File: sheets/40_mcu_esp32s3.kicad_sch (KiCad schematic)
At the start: 20 parts, among them J401 USB4105-GF-A, J402 UART0, SW401 RESET, SW402 BOOT, U401 ESP32-S3-WROOM-1-N8R2, U402 USBLC6-2SC6

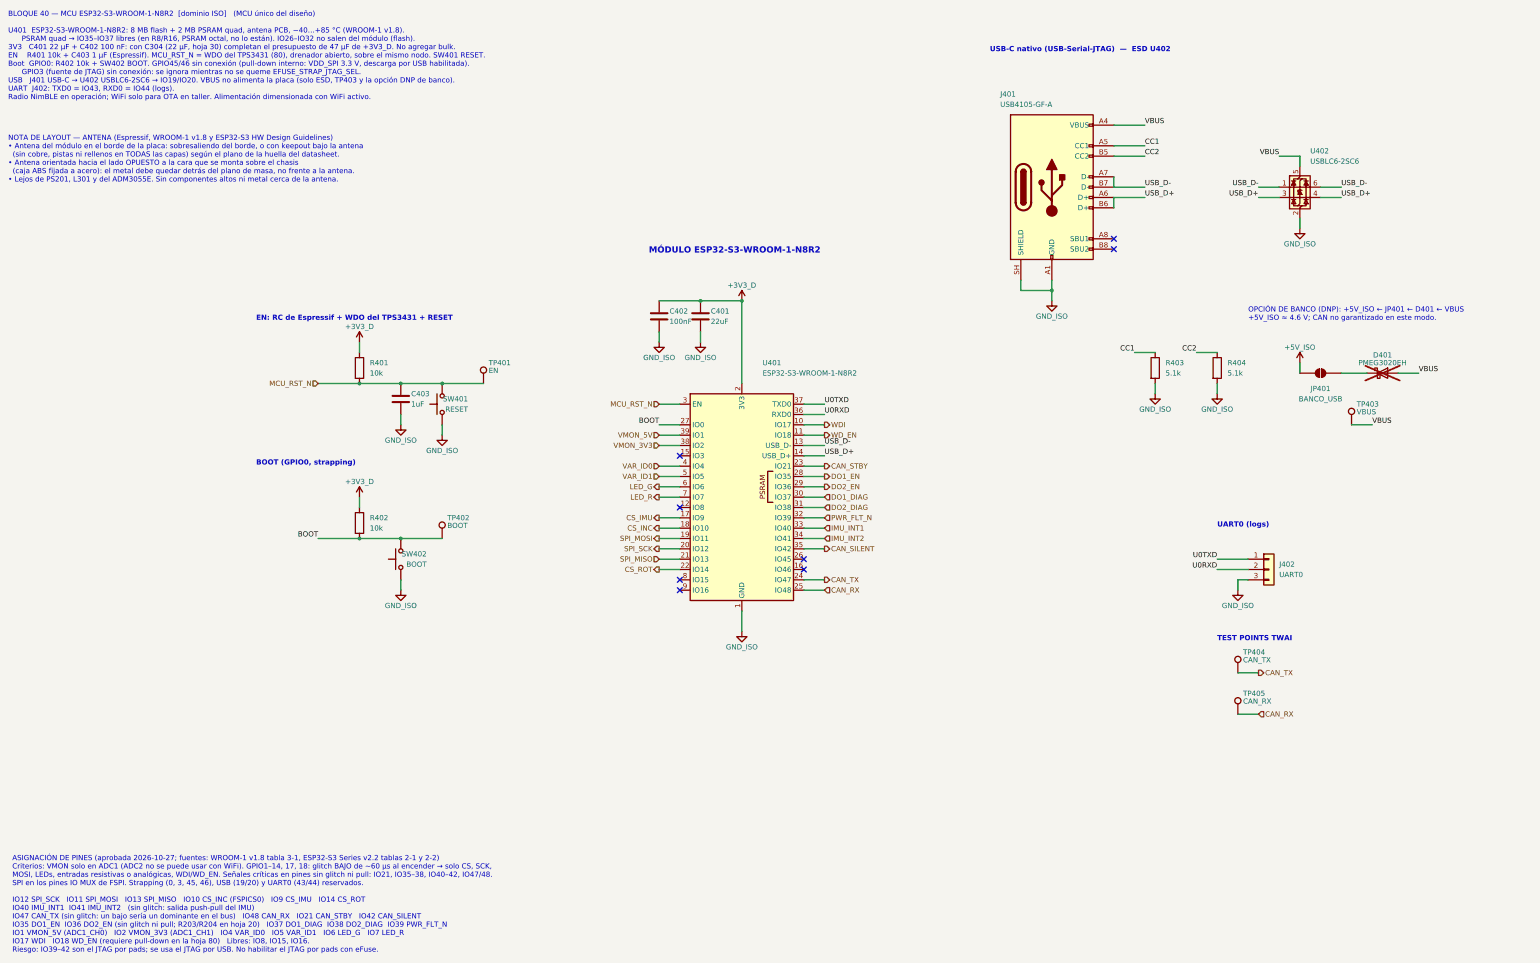
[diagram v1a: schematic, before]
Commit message: [Claude Code] 20_buck_5v: opción B (no aislada) con LMR38010; masas unificadas
- sheets/20_isolation -> sheets/20_buck_5v: se quitan PS201, ISO7763 y
  TPS7A1650; U201 LMR38010SQDDARQ1 (PROTO: LMR38010SDDAR, LCSC C5219310),
  5.02 V / 1 A a 400 kHz según TI SNVSC73B (L201 XAL6060-333, 3 x 22 uF,
  RT 64.9k, FB 100k/24.9k). Huella oficial HSOIC-8 con vías térmicas.
- Símbolo LMR38010 (easyeda2kicad) en lib/easyeda2kicad/INCLI-VA_easyeda,
  con tipos de pin ajustados; registrado en sym-lib-table.
- Todas las hojas: GND_ISO -> GND_VEH, +5V_ISO -> +5V_VEH.
- Raíz: EN/DIAG/FLT directos entre las hojas 40, 70 y 10; la hoja 20 sin pines.
- 10_power_input: R111 a +3V3_D, C109 = 100 nF (inrush con C105),
  C105 DNP solo en PROTO; se quita un PWR_FLAG suelto en GND_VEH.
- 70_output_ch: cambios de layout del usuario (hechos en KiCad).
- Textos de las hojas 30/40/50/80 y la raíz sin referencias al aislamiento.
- ERC: 0 en 10, 20, 30, 40, 50, 60 y 70; quedan los de 80 (hoja vacía).

Co-Authored-By: Claude Opus 5.5 <noreply@anthropic.com>
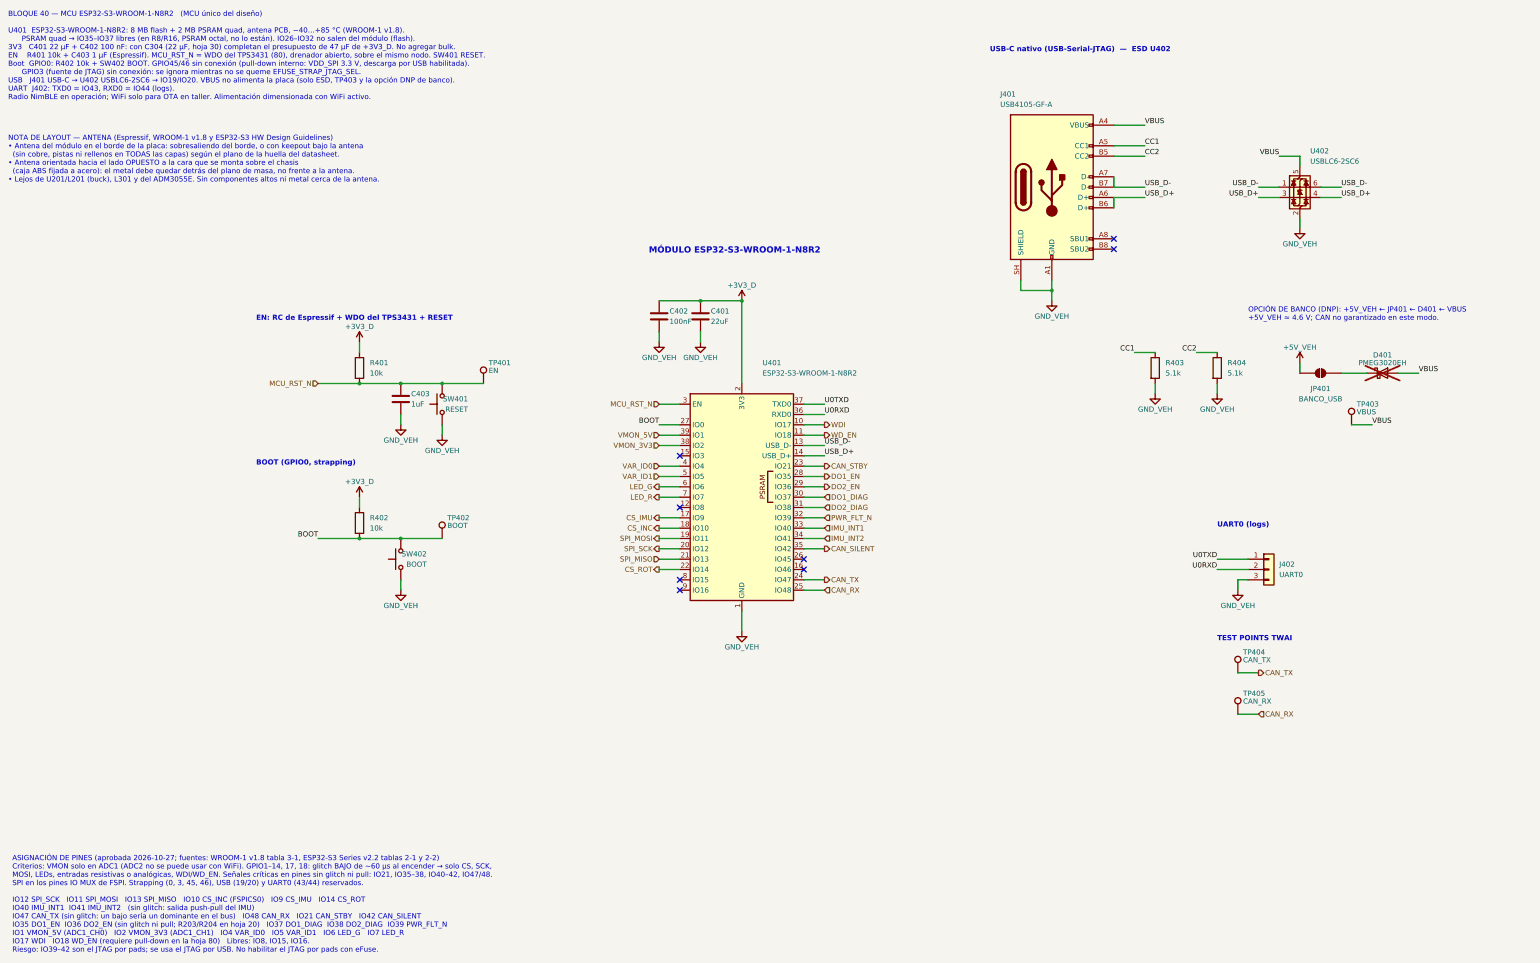
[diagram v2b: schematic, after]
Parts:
- D401: Notes DNP. Opción de banco: alimenta +5V_ISO desde VBUS para flas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 -> DNP. Opción de banco: alimenta +5V_VEH desde VBUS para flas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
- J401: Notes USB-C solo USB 2.0 para el USB-Serial-JTAG del ESP32-S3 (GPIO19/20). Programación, consola y JTAG. Masa = GND_ISO: la PC queda aislada del vehículo por la barrera 1. Blindaje a GND_ISO. -> USB-C solo USB 2.0 para el USB-Serial-JTAG del ESP32-S3 (GPIO19/20). Programación, consola y JTAG. Masa = GND_VEH: SIN aislamiento (opción B), la PC comparte masa con el vehículo; en el vehículo usar aislador USB/UART o laptop a batería. Blindaje a GND_VEH.
- J402: Notes UART0 para logs: 1 = TXD0 (IO43, sale del MCU), 2 = RXD0 (IO44), 3 = GND_ISO. Adaptador USB-UART de 3.3 V. -> UART0 para logs: 1 = TXD0 (IO43, sale del MCU), 2 = RXD0 (IO44), 3 = GND_VEH. Adaptador USB-UART de 3.3 V.
- JP401: Notes Abierto de fábrica. Cerrar solo en el banco, junto con D401, para alimentar +5V_ISO desde USB. Abrir antes de instalar en el vehículo. -> Abierto de fábrica. Cerrar solo en el banco, junto con D401, para alimentar +5V_VEH desde USB. Abrir antes de instalar en el vehículo.
- SW401: Notes Botón RESET: lleva EN a GND_ISO. THT 6 x 6 mm, fácil de sol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 -> Botón RESET: lleva EN a GND_VEH. THT 6 x 6 mm, fácil de sol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
- SW402: Notes Botón BOOT: GPIO0 a GND_ISO. Mantener apretado y soltar RES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 -> Botón BOOT: GPIO0 a GND_VEH. Mantener apretado y soltar RES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
- U401: Notes 8 MB flash quad + 2 MB PSRAM quad, antena PCB, -40 a +85 C (las variantes R8/R16 con PSRAM octal llegan solo a 65 C). PSRAM quad: IO35-IO37 libres (WROOM-1 v1.8, tabla 3-1, nota b). LCSC C2913204. Pad 41 (EPAD) y pines 1/40 a GND_ISO. Antena al borde de la placa con keepout (ver nota de layout). -> 8 MB flash quad + 2 MB PSRAM quad, antena PCB, -40 a +85 C (las variantes R8/R16 con PSRAM octal llegan solo a 65 C). PSRAM quad: IO35-IO37 libres (WROOM-1 v1.8, tabla 3-1, nota b). LCSC C2913204. Pad 41 (EPAD) y pines 1/40 a GND_VEH. Antena al borde de la placa con keepout (ver nota de layout).
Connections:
- net +5V_ISO renamed +5V_VEH
- net GND_ISO renamed GND_VEH
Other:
- note added: "BLOQUE 40 — MCU ESP32-S3-WROOM-1-N8R2 (MCU único del diseño) U401 ESP32-S3-WROOM-1-N8R2: 8 MB flash + 2 MB PSRAM quad, antena PCB, −40…+85 °C (WROOM-1 v1.8). PSRAM quad → IO35–IO37 libres (en R8/R16, PSRAM octal, no lo están). IO26–IO32 no salen del módulo (flash). 3V3 C401 22 µF + C402 100 nF: con C304 (22 µF, hoja 30) completan el presupuesto de 47 µF de +3V3_D. No agregar bulk. EN R401 10k + C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"
- note added: "OPCIÓN DE BANCO (DNP): +5V_VEH ← JP401 ← D401 ← VBUS +5V_VEH ≈ 4.6 V; CAN no garantizado en este modo."
- note removed: "BLOQUE 40 — MCU ESP32-S3-WROOM-1-N8R2 [dominio ISO] (MCU único del diseño) U401 ESP32-S3-WROOM-1-N8R2: 8 MB flash + 2 MB PSRAM quad, antena PCB, −40…+85 °C (WROOM-1 v1.8). PSRAM quad → IO35–IO37 libres (en R8/R16, PSRAM octal, no lo están). IO26–IO32 no salen del módulo (flash). 3V3 C401 22 µF + C402 100 nF: con C304 (22 µF, hoja 30) completan el presupuesto de 47 µF de +3V3_D. No agregar bulk. E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"
- note removed: "OPCIÓN DE BANCO (DNP): +5V_ISO ← JP401 ← D401 ← VBUS +5V_ISO ≈ 4.6 V; CAN no garantizado en este modo."
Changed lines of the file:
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@@
 		)
 	)
-	(text "OPCIÓN DE BANCO (DNP): +5V_ISO ← JP401 ← D401 ← VBUS\n+5V_ISO ≈ 4.6 V; CAN no garantizado en este modo."
+	(text "OPCIÓN DE BANCO (DNP): +5V_VEH ← JP401 ← D401 ← VBUS\n+5V_VEH ≈ 4.6 V; CAN no garantizado en este modo."
 		(exclude_from_sim no)
 		(at 325.12 96.52 0)
@@
 		)
 	)
-	(text "NOTA DE LAYOUT — ANTENA (Espressif, WROOM-1 v1.8 y ESP32-S3 HW Design Guidelines)\n• Antena del módulo en el borde de la placa: sobresaliendo del borde, o con keepout bajo la antena\n  (sin cobre, pistas ni rellenos en TODAS las capas) según el plano de la huella del datasheet.\n• Antena orientada hacia el lado OPUESTO a la cara que se monta sobre el chasis\n  (caja ABS fijada a acero): el metal debe quedar detrás del plano de masa, no frente a la antena.\n• Lejos de PS201, L301 y del ADM3055E. Sin componentes altos ni metal cerca de la antena."
+	(text "NOTA DE LAYOUT — ANTENA (Espressif, WROOM-1 v1.8 y ESP32-S3 HW Design Guidelines)\n• Antena del módulo en el borde de la placa: sobresaliendo del borde, o con keepout bajo la antena\n  (sin cobre, pistas ni rellenos en TODAS las capas) según el plano de la huella del datasheet.\n• Antena orientada hacia el lado OPUESTO a la cara que se monta sobre el chasis\n  (caja ABS fijada a acero): el metal debe quedar detrás del plano de masa, no frente a la antena.\n• Lejos de U201/L201 (buck), L301 y del ADM3055E. Sin componentes altos ni metal cerca de la antena."
 		(exclude_from_sim no)
 		(at 20.32 50.8 0)
@@
 		)
 	)
-	(text "BLOQUE 40 — MCU ESP32-S3-WROOM-1-N8R2  [dominio ISO]   (MCU único del diseño)\n\nU401  ESP32-S3-WROOM-1-N8R2: 8 MB flash + 2 MB PSRAM quad, antena PCB, −40…+85 °C (WROOM-1 v1.8).\n      PSRAM quad → IO35–IO37 libres (en R8/R16, PSRAM octal, no lo están). IO26–IO32 no salen del módulo (flash).\n3V3   C401 22 µF + C402 100 nF: con C304 (22 µF, hoja 30) completan el presupuesto de 47 µF de +3V3_D. No agregar bulk.\nEN    R401 10k + C403 1 µF (Espressif). MCU_RST_N = WDO del TPS3431 (80), drenador abierto, sobre el mismo nodo. SW401 RESET.\nBoot  GPIO0: R402 10k + SW402 BOOT. GPIO45/46 sin conexión (pull-down interno: VDD_SPI 3.3 V, descarga por USB habilitada).\n      GPIO3 (fuente de JTAG) sin conexión: se ignora mientras no se queme EFUSE_STRAP_JTAG_SEL.\nUSB   J401 USB-C → U402 USBLC6-2SC6 → IO19/IO20. VBUS no alimenta la placa (solo ESD, TP403 y la opción DNP de banco).\nUART  J402: TXD0 = IO43, RXD0 = IO44 (logs).\nRadio NimBLE en operación; WiFi solo para OTA en taller. Alimentación dimensionada con WiFi activo."
+	(text "BLOQUE 40 — MCU ESP32-S3-WROOM-1-N8R2   (MCU único del diseño)\n\nU401  ESP32-S3-WROOM-1-N8R2: 8 MB flash + 2 MB PSRAM quad, antena PCB, −40…+85 °C (WROOM-1 v1.8).\n      PSRAM quad → IO35–IO37 libres (en R8/R16, PSRAM octal, no lo están). IO26–IO32 no salen del módulo (flash).\n3V3   C401 22 µF + C402 100 nF: con C304 (22 µF, hoja 30) completan el presupuesto de 47 µF de +3V3_D. No agregar bulk.\nEN    R401 10k + C403 1 µF (Espressif). MCU_RST_N = WDO del TPS3431 (80), drenador abierto, sobre el mismo nodo. SW401 RESET.\nBoot  GPIO0: R402 10k + SW402 BOOT. GPIO45/46 sin conexión (pull-down interno: VDD_SPI 3.3 V, descarga por USB habilitada).\n      GPIO3 (fuente de JTAG) sin conexión: se ignora mientras no se queme EFUSE_STRAP_JTAG_SEL.\nUSB   J401 USB-C → U402 USBLC6-2SC6 → IO19/IO20. VBUS no alimenta la placa (solo ESD, TP403 y la opción DNP de banco).\nUART  J402: TXD0 = IO43, RXD0 = IO44 (logs).\nRadio NimBLE en operación; WiFi solo para OTA en taller. Alimentación dimensionada con WiFi activo."
 		(exclude_from_sim no)
 		(at 20.32 20.32 0)
@@
 	)
 	(symbol
-		(lib_id "INCLI-VA:GND_ISO")
+		(lib_id "INCLI-VA:GND_VEH")
 		(at 322.58 162.56 0)
 		(unit 1)
@@
 			)
 		)
-		(property "Value" "GND_ISO"
+		(property "Value" "GND_VEH"
 			(at 322.58 166.37 0)
 			(show_name no)
@@
 	)
 	(symbol
-		(lib_id "INCLI-VA:GND_ISO")
+		(lib_id "INCLI-VA:GND_VEH")
 		(at 116.84 121.92 0)
 		(unit 1)
@@
 			)
 		)
-		(property "Value" "GND_ISO"
+		(property "Value" "GND_VEH"
 			(at 116.84 125.73 0)
 			(show_name no)
@@
 	)
 	(symbol
-		(lib_id "INCLI-VA:GND_ISO")
+		(lib_id "INCLI-VA:GND_VEH")
 		(at 200.66 172.72 0)
 		(unit 1)
@@
 			)
 		)
-		(property "Value" "GND_ISO"
+		(property "Value" "GND_VEH"
 			(at 200.66 176.53 0)
 			(show_name no)
@@
 	)
 	(symbol
-		(lib_id "INCLI-VA:GND_ISO")
+		(lib_id "INCLI-VA:GND_VEH")
 		(at 317.5 114.3 0)
 		(unit 1)
@@
 			)
 		)
-		(property "Value" "GND_ISO"
+		(property "Value" "GND_VEH"
 			(at 317.5 118.11 0)
 			(show_name no)
@@
 	)
 	(symbol
-		(lib_id "INCLI-VA:GND_ISO")
+		(lib_id "INCLI-VA:GND_VEH")
 		(at 180.34 101.6 0)
 		(unit 1)
@@
 			)
 		)
-		(property "Value" "GND_ISO"
+		(property "Value" "GND_VEH"
 			(at 180.34 105.41 0)
 			(show_name no)
@@
 			)
 		)
-		(property "Notes" "8 MB flash quad + 2 MB PSRAM quad, antena PCB, -40 a +85 C (las variantes R8/R16 con PSRAM octal llegan solo a 65 C). PSRAM quad: IO35-IO37 libres (WROOM-1 v1.8, tabla 3-1, nota b). LCSC C2913204. Pad 41 (EPAD) y pines 1/40 a GND_ISO. Antena al borde de la placa con keepout (ver nota de layout)."
+		(property "Notes" "8 MB flash quad + 2 MB PSRAM quad, antena PCB, -40 a +85 C (las variantes R8/R16 con PSRAM octal llegan solo a 65 C). PSRAM quad: IO35-IO37 libres (WROOM-1 v1.8, tabla 3-1, nota b). LCSC C2913204. Pad 41 (EPAD) y pines 1/40 a GND_VEH. Antena al borde de la placa con keepout (ver nota de layout)."
 			(at 200.66 139.7 0)
 			(hide yes)
@@
 			)
 		)
-		(property "Notes" "Botón BOOT: GPIO0 a GND_ISO. Mantener apretado y soltar RESET para entrar en descarga."
+		(property "Notes" "Botón BOOT: GPIO0 a GND_VEH. Mantener apretado y soltar RESET para entrar en descarga."
 			(at 116.84 154.94 0)
 			(hide yes)
@@
 			)
 		)
-		(property "Notes" "DNP. Opción de banco: alimenta +5V_ISO desde VBUS para flashear sin vehículo (cerrar JP401). +5V_ISO queda en ~4.6 V: el CAN (ADM3055E, VCC mín. 4.5 V) no está garantizado en este modo. Limitar la carga a lo que entrega el puerto (WiFi apagado). Con PS201 activo el diodo queda en inversa. MPN a verificar (disponibilidad y especificación) antes de congelar el BOM."
+		(property "Notes" "DNP. Opción de banco: alimenta +5V_VEH desde VBUS para flashear sin vehículo (cerrar JP401). +5V_VEH queda en ~4.6 V: el CAN (ADM3055E, VCC mín. 4.5 V) no está garantizado en este modo. Limitar la carga a lo que entrega el puerto (WiFi apagado). Con el buck activo el diodo queda en inversa. MPN a verificar (disponibilidad y especificación) antes de congelar el BOM."
 			(at 358.14 109.22 0)
 			(hide yes)
@@
 			)
 		)
-		(property "Notes" "Abierto de fábrica. Cerrar solo en el banco, junto con D401, para alimentar +5V_ISO desde USB. Abrir antes de instalar en el vehículo."
+		(property "Notes" "Abierto de fábrica. Cerrar solo en el banco, junto con D401, para alimentar +5V_VEH desde USB. Abrir antes de instalar en el vehículo."
 			(at 342.9 109.22 0)
 			(hide yes)
@@
 	)
 	(symbol
-		(lib_id "INCLI-VA:GND_ISO")
+		(lib_id "INCLI-VA:GND_VEH")
 		(at 190.5 101.6 0)
 		(unit 1)
@@
 			)
 		)
-		(property "Value" "GND_ISO"
+		(property "Value" "GND_VEH"
 			(at 190.5 105.41 0)
 			(show_name no)
@@
 			)
 		)
-		(property "Notes" "UART0 para logs: 1 = TXD0 (IO43, sale del MCU), 2 = RXD0 (IO44), 3 = GND_ISO. Adaptador USB-UART de 3.3 V."
+		(property "Notes" "UART0 para logs: 1 = TXD0 (IO43, sale del MCU), 2 = RXD0 (IO44), 3 = GND_VEH. Adaptador USB-UART de 3.3 V."
 			(at 330.2 157.48 0)
 			(hide yes)
@@
 	)
 	(symbol
-		(lib_id "INCLI-VA:GND_ISO")
+		(lib_id "INCLI-VA:GND_VEH")
 		(at 276.86 91.44 0)
 		(unit 1)
@@
 			)
 		)
-		(property "Value" "GND_ISO"
+		(property "Value" "GND_VEH"
 			(at 276.86 95.25 0)
 			(show_name no)
@@
 			)
 		)
-		(property "Notes" "Botón RESET: lleva EN a GND_ISO. THT 6 x 6 mm, fácil de soldar a mano."
+		(property "Notes" "Botón RESET: lleva EN a GND_VEH. THT 6 x 6 mm, fácil de soldar a mano."
 			(at 127 116.84 0)
 			(hide yes)
@@
 	)
 	(symbol
-		(lib_id "INCLI-VA:GND_ISO")
+		(lib_id "INCLI-VA:GND_VEH")
 		(at 127 124.46 0)
 		(unit 1)
@@
 			)
 		)
-		(property "Value" "GND_ISO"
+		(property "Value" "GND_VEH"
 			(at 127 128.27 0)
 			(show_name no)
@@
 	)
 	(symbol
-		(lib_id "INCLI-VA:GND_ISO")
+		(lib_id "INCLI-VA:GND_VEH")
 		(at 116.84 162.56 0)
 		(unit 1)
@@
 			)
 		)
-		(property "Value" "GND_ISO"
+		(property "Value" "GND_VEH"
 			(at 116.84 166.37 0)
 			(show_name no)
@@
 	)
 	(symbol
-		(lib_id "INCLI-VA:GND_ISO")
+		(lib_id "INCLI-VA:GND_VEH")
 		(at 302.26 114.3 0)
 		(unit 1)
@@
 			)
 		)
-		(property "Value" "GND_ISO"
+		(property "Value" "GND_VEH"
 			(at 302.26 118.11 0)
 			(show_name no)
@@
 	)
 	(symbol
-		(lib_id "INCLI-VA:+5V_ISO")
+		(lib_id "INCLI-VA:+5V_VEH")
 		(at 337.82 106.68 0)
 		(unit 1)
@@
 			)
 		)
-		(property "Value" "+5V_ISO"
+		(property "Value" "+5V_VEH"
 			(at 337.82 102.87 0)
 			(show_name no)
@@
 	)
 	(symbol
-		(lib_id "INCLI-VA:GND_ISO")
+		(lib_id "INCLI-VA:GND_VEH")
 		(at 337.82 73.66 0)
 		(unit 1)
@@
 			)
 		)
-		(property "Value" "GND_ISO"
+		(property "Value" "GND_VEH"
 			(at 337.82 77.47 0)
 			(show_name no)
@@
 			)
 		)
-		(property "Notes" "USB-C solo USB 2.0 para el USB-Serial-JTAG del ESP32-S3 (GPIO19/20). Programación, consola y JTAG. Masa = GND_ISO: la PC queda aislada del vehículo por la barrera 1. Blindaje a GND_ISO."
+		(property "Notes" "USB-C solo USB 2.0 para el USB-Serial-JTAG del ESP32-S3 (GPIO19/20). Programación, consola y JTAG. Masa = GND_VEH: SIN aislamiento (opción B), la PC comparte masa con el vehículo; en el vehículo usar aislador USB/UART o laptop a batería. Blindaje a GND_VEH."
 			(at 276.86 63.5 0)
 			(hide yes)
